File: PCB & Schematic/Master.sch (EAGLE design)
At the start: 24 parts, among them IC1 MAX705CUA, M1 ARDUINO_R3_ICSP_NODIM, X1 MAB5SH, X2 MAB5SH

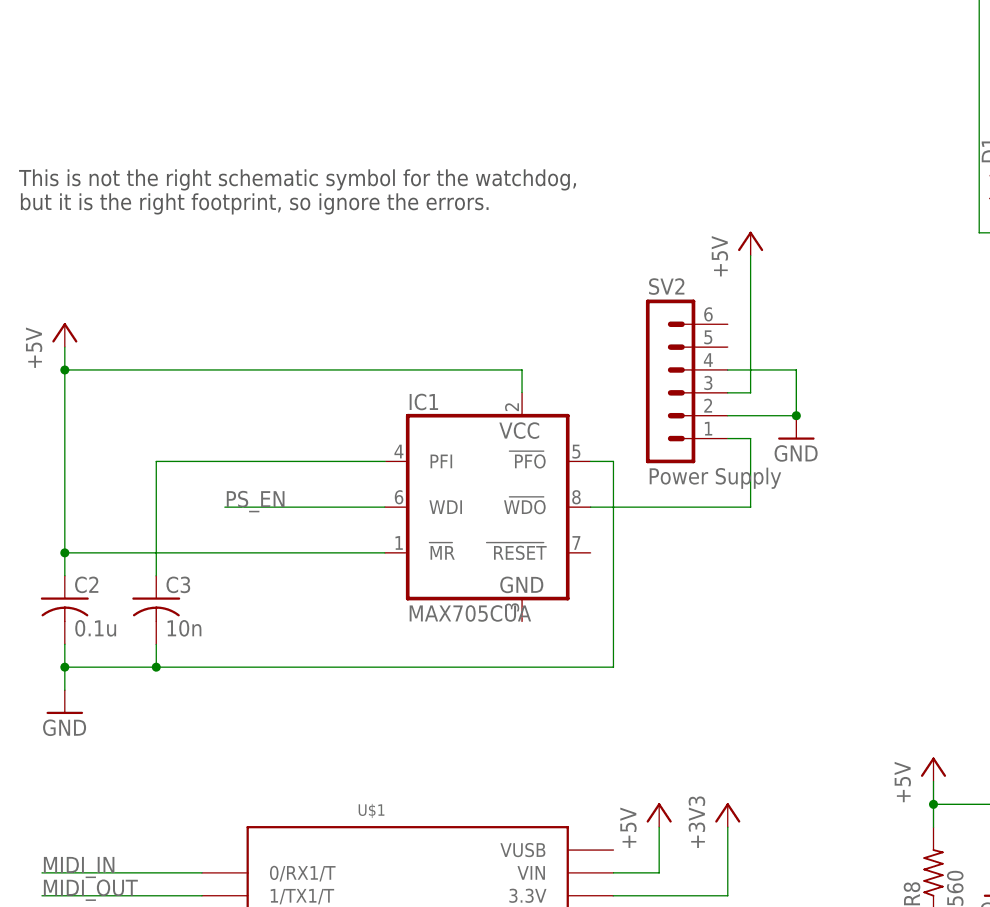
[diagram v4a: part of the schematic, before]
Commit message: Make the correct part for the watchdog.
This is much cleaner.
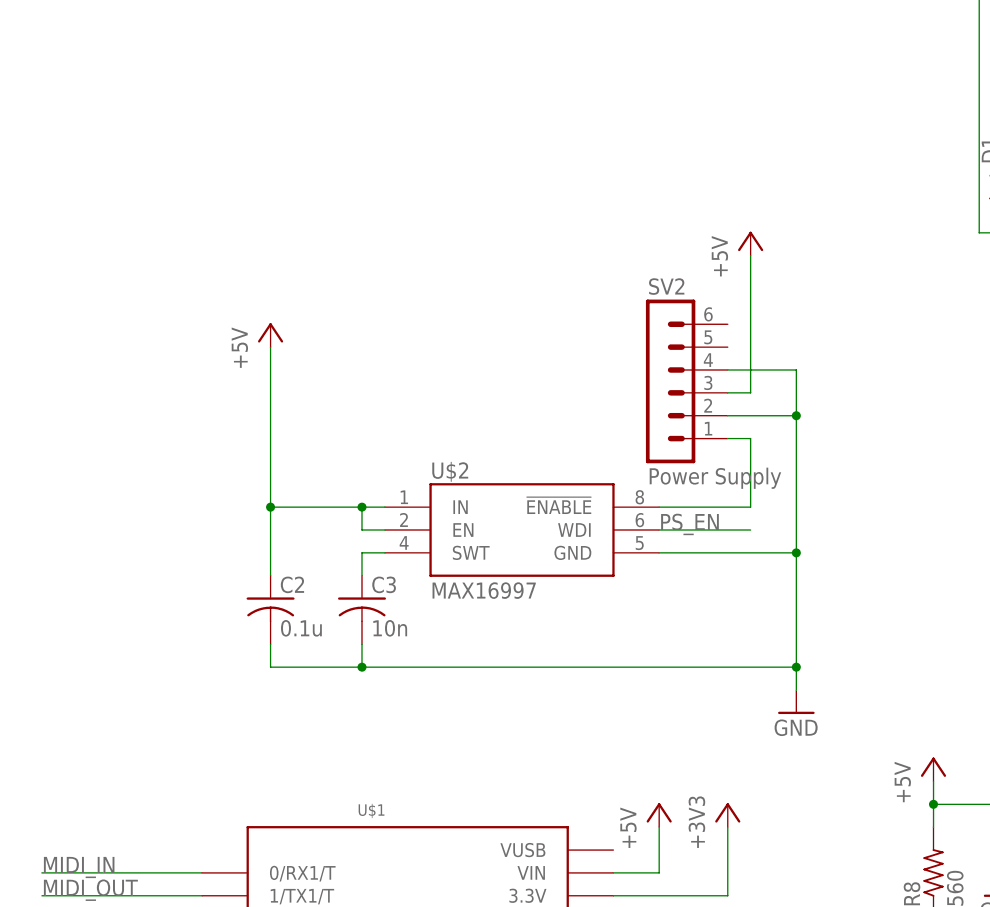
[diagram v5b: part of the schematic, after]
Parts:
- removed IC1: MAX705CUA, maxim:MAX705CUA
- added U$2: MAX16997, DAVe3283:MAX16997
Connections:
- removed net N$15: C3.1, IC1.PFI
- new net N$8: C3.1, U$2.SWT
- net +5V: now also U$2.EN, U$2.IN; no longer IC1.MR, IC1.VCC
- net GND: now also U$2.GND; no longer IC1.PFO
- net N$11: now also U$2.!ENABLE; no longer IC1.WDO
- net PS_EN: now also U$2.WDI; no longer IC1.WDI
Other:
- note removed: "This is not the right schematic symbol for the watchdog, but it is the right footprint, so ignore the errors."
- moved on the sheet: C2, C3
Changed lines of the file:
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@@
 <part name="GND5" library="supply1" deviceset="GNDINT" device=""/>
 <part name="SV2" library="con-lstb" deviceset="MA06-1" device="" value="Power Supply"/>
-<part name="GND6" library="supply1" deviceset="GND" device=""/>
 <part name="P+4" library="supply1" deviceset="+5V" device=""/>
-<part name="IC1" library="maxim" deviceset="MAX705CUA" device=""/>
 <part name="P+7" library="supply1" deviceset="+5V" device=""/>
 <part name="C2" library="resistor" deviceset="C-US" device="C0805" value="0.1u"/>
 <part name="GND7" library="supply1" deviceset="GND" device=""/>
 <part name="C3" library="resistor" deviceset="C-US" device="C0805" value="10n"/>
+<part name="U$2" library="DAVe3283" deviceset="MAX16997" device=""/>
 </parts>
 <sheets>
 <sheet>
 <plain>
-<text x="0" y="139.7" size="1.778" layer="97">This is not the right schematic symbol for the watchdog,
-but it is the right footprint, so ignore the errors.</text>
 </plain>
 <instances>
@@
 <instance part="GND5" gate="G$1" x="147.32" y="35.56"/>
 <instance part="SV2" gate="1" x="71.12" y="121.92"/>
-<instance part="GND6" gate="1" x="86.36" y="114.3"/>
 <instance part="P+4" gate="1" x="81.28" y="137.16"/>
-<instance part="IC1" gate="G$1" x="50.8" y="106.68"/>
-<instance part="P+7" gate="1" x="5.08" y="127"/>
-<instance part="C2" gate="G$1" x="5.08" y="96.52"/>
-<instance part="GND7" gate="1" x="5.08" y="83.82"/>
-<instance part="C3" gate="G$1" x="15.24" y="96.52"/>
+<instance part="P+7" gate="1" x="27.94" y="127"/>
+<instance part="C2" gate="G$1" x="27.94" y="96.52"/>
+<instance part="GND7" gate="1" x="86.36" y="83.82"/>
+<instance part="C3" gate="G$1" x="38.1" y="96.52"/>
+<instance part="U$2" gate="G$1" x="55.88" y="104.14"/>
 </instances>
 <busses>
@@
 </segment>
 <segment>
-<pinref part="GND6" gate="1" pin="GND"/>
+<pinref part="C2" gate="G$1" pin="2"/>
+<wire x1="38.1" y1="88.9" x2="27.94" y2="88.9" width="0.1524" layer="91"/>
+<wire x1="27.94" y1="88.9" x2="27.94" y2="91.44" width="0.1524" layer="91"/>
+<pinref part="C3" gate="G$1" pin="2"/>
+<wire x1="38.1" y1="91.44" x2="38.1" y2="88.9" width="0.1524" layer="91"/>
 <pinref part="SV2" gate="1" pin="2"/>
 <wire x1="86.36" y1="116.84" x2="78.74" y2="116.84" width="0.1524" layer="91"/>
-<junction x="86.36" y="116.84"/>
 <pinref part="SV2" gate="1" pin="4"/>
 <wire x1="78.74" y1="121.92" x2="86.36" y2="121.92" width="0.1524" layer="91"/>
 <wire x1="86.36" y1="121.92" x2="86.36" y2="116.84" width="0.1524" layer="91"/>
-</segment>
-<segment>
-<pinref part="IC1" gate="G$1" pin="PFO"/>
-<wire x1="63.5" y1="111.76" x2="66.04" y2="111.76" width="0.1524" layer="91"/>
-<wire x1="66.04" y1="111.76" x2="66.04" y2="88.9" width="0.1524" layer="91"/>
-<pinref part="C2" gate="G$1" pin="2"/>
-<wire x1="66.04" y1="88.9" x2="15.24" y2="88.9" width="0.1524" layer="91"/>
-<wire x1="15.24" y1="88.9" x2="5.08" y2="88.9" width="0.1524" layer="91"/>
-<wire x1="5.08" y1="88.9" x2="5.08" y2="91.44" width="0.1524" layer="91"/>
-<wire x1="5.08" y1="86.36" x2="5.08" y2="88.9" width="0.1524" layer="91"/>
-<junction x="5.08" y="88.9"/>
+<pinref part="U$2" gate="G$1" pin="GND"/>
+<wire x1="71.12" y1="101.6" x2="86.36" y2="101.6" width="0.1524" layer="91"/>
+<wire x1="86.36" y1="101.6" x2="86.36" y2="116.84" width="0.1524" layer="91"/>
+<junction x="86.36" y="116.84"/>
+<wire x1="38.1" y1="88.9" x2="86.36" y2="88.9" width="0.1524" layer="91"/>
+<wire x1="86.36" y1="88.9" x2="86.36" y2="101.6" width="0.1524" layer="91"/>
+<junction x="38.1" y="88.9"/>
+<junction x="86.36" y="101.6"/>
 <pinref part="GND7" gate="1" pin="GND"/>
-<pinref part="C3" gate="G$1" pin="2"/>
-<wire x1="15.24" y1="91.44" x2="15.24" y2="88.9" width="0.1524" layer="91"/>
-<junction x="15.24" y="88.9"/>
+<wire x1="86.36" y1="86.36" x2="86.36" y2="88.9" width="0.1524" layer="91"/>
+<junction x="86.36" y="88.9"/>
 </segment>
 </net>
@@
 <pinref part="P+7" gate="1" pin="+5V"/>
 <pinref part="C2" gate="G$1" pin="1"/>
-<wire x1="5.08" y1="124.46" x2="5.08" y2="121.92" width="0.1524" layer="91"/>
-<pinref part="IC1" gate="G$1" pin="MR"/>
-<wire x1="5.08" y1="121.92" x2="5.08" y2="101.6" width="0.1524" layer="91"/>
-<wire x1="5.08" y1="101.6" x2="5.08" y2="99.06" width="0.1524" layer="91"/>
-<wire x1="40.64" y1="101.6" x2="5.08" y2="101.6" width="0.1524" layer="91"/>
-<junction x="5.08" y="101.6"/>
-<pinref part="IC1" gate="G$1" pin="VCC"/>
-<wire x1="55.88" y1="119.38" x2="55.88" y2="121.92" width="0.1524" layer="91"/>
-<wire x1="55.88" y1="121.92" x2="5.08" y2="121.92" width="0.1524" layer="91"/>
-<junction x="5.08" y="121.92"/>
+<wire x1="27.94" y1="124.46" x2="27.94" y2="106.68" width="0.1524" layer="91"/>
+<pinref part="U$2" gate="G$1" pin="IN"/>
+<wire x1="27.94" y1="106.68" x2="27.94" y2="99.06" width="0.1524" layer="91"/>
+<wire x1="40.64" y1="106.68" x2="38.1" y2="106.68" width="0.1524" layer="91"/>
+<junction x="27.94" y="106.68"/>
+<pinref part="U$2" gate="G$1" pin="EN"/>
+<wire x1="38.1" y1="106.68" x2="27.94" y2="106.68" width="0.1524" layer="91"/>
+<wire x1="40.64" y1="104.14" x2="38.1" y2="104.14" width="0.1524" layer="91"/>
+<wire x1="38.1" y1="104.14" x2="38.1" y2="106.68" width="0.1524" layer="91"/>
+<junction x="38.1" y="106.68"/>
 </segment>
 </net>
@@
 </segment>
 <segment>
-<pinref part="IC1" gate="G$1" pin="WDI"/>
-<wire x1="40.64" y1="106.68" x2="22.86" y2="106.68" width="0.1524" layer="91"/>
-<label x="22.86" y="106.68" size="1.778" layer="95"/>
+<wire x1="81.28" y1="104.14" x2="71.12" y2="104.14" width="0.1524" layer="91"/>
+<label x="71.12" y="104.14" size="1.778" layer="95"/>
+<pinref part="U$2" gate="G$1" pin="WDI"/>
 </segment>
 <segment>
@@
 </segment>
 </net>
-<net name="N$15" class="0">
-<segment>
-<pinref part="C3" gate="G$1" pin="1"/>
-<wire x1="15.24" y1="99.06" x2="15.24" y2="111.76" width="0.1524" layer="91"/>
-<pinref part="IC1" gate="G$1" pin="PFI"/>
-<wire x1="15.24" y1="111.76" x2="40.64" y2="111.76" width="0.1524" layer="91"/>
-</segment>
-</net>
 <net name="N$11" class="0">
 <segment>
-<pinref part="IC1" gate="G$1" pin="WDO"/>
-<wire x1="63.5" y1="106.68" x2="81.28" y2="106.68" width="0.1524" layer="91"/>
 <wire x1="81.28" y1="106.68" x2="81.28" y2="114.3" width="0.1524" layer="91"/>
 <pinref part="SV2" gate="1" pin="1"/>
 <wire x1="81.28" y1="114.3" x2="78.74" y2="114.3" width="0.1524" layer="91"/>
+<pinref part="U$2" gate="G$1" pin="!ENABLE"/>
+<wire x1="71.12" y1="106.68" x2="81.28" y2="106.68" width="0.1524" layer="91"/>
+</segment>
+</net>
+<net name="N$8" class="0">
+<segment>
+<pinref part="U$2" gate="G$1" pin="SWT"/>
+<pinref part="C3" gate="G$1" pin="1"/>
+<wire x1="40.64" y1="101.6" x2="38.1" y2="101.6" width="0.1524" layer="91"/>
+<wire x1="38.1" y1="101.6" x2="38.1" y2="99.06" width="0.1524" layer="91"/>
 </segment>
 </net>
@@
 </schematic>
 </drawing>
-<compatibility>
-<note version="6.3" minversion="6.2.2" severity="warning">
-Since Version 6.2.2 text objects can contain more than one line,
-which will not be processed correctly with this version.
-</note>
-</compatibility>
 </eagle>

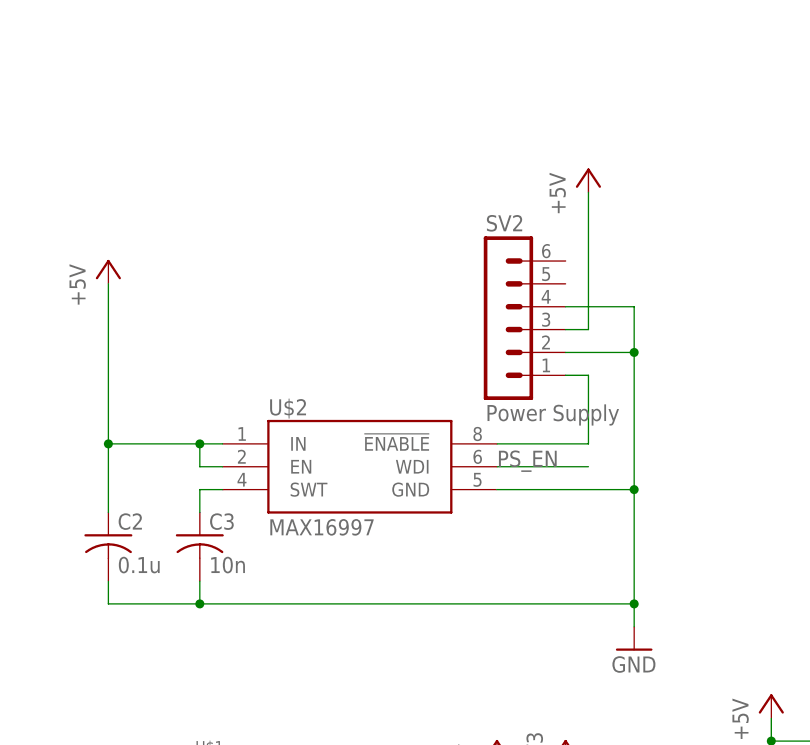
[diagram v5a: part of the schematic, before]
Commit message: Power connector now 4 pin. Add doorbell notes.
The 6 pin connector was unnecessary, and risked confusion with the
slave board connector.

Added some notes on the cheap wireless doorbell I bought to
integrate with the chimes.
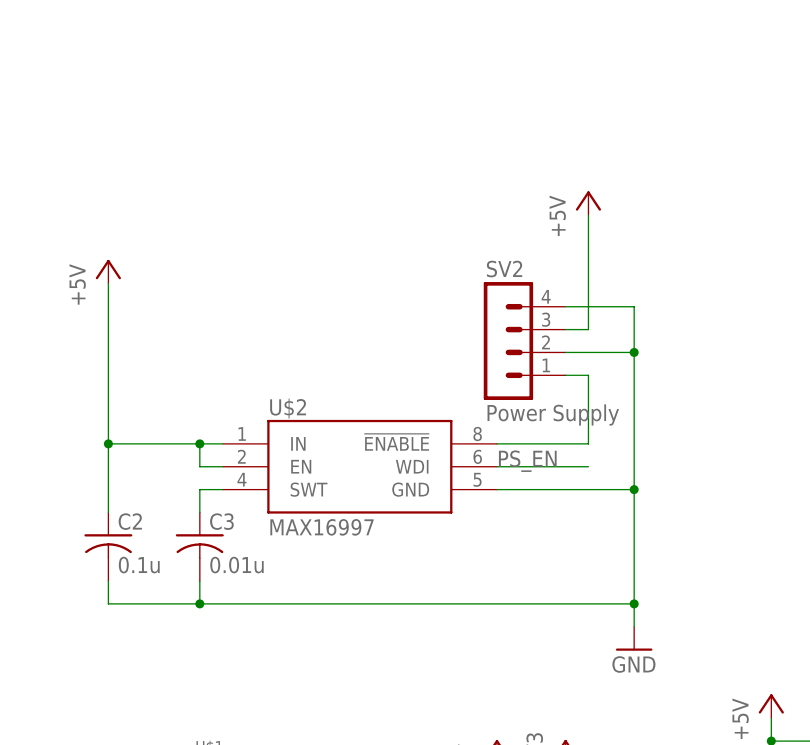
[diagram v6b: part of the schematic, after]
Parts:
- C3: value 10n -> 0.01u
- SV2: device con-lstb:MA06-1 -> con-lstb:MA04-1
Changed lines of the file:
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@@
 <part name="VCC1" library="supply1" deviceset="VCCINT" device=""/>
 <part name="GND5" library="supply1" deviceset="GNDINT" device=""/>
-<part name="SV2" library="con-lstb" deviceset="MA06-1" device="" value="Power Supply"/>
+<part name="SV2" library="con-lstb" deviceset="MA04-1" device="" value="Power Supply"/>
 <part name="P+4" library="supply1" deviceset="+5V" device=""/>
 <part name="P+7" library="supply1" deviceset="+5V" device=""/>
 <part name="C2" library="resistor" deviceset="C-US" device="C0805" value="0.1u"/>
 <part name="GND7" library="supply1" deviceset="GND" device=""/>
-<part name="C3" library="resistor" deviceset="C-US" device="C0805" value="10n"/>
+<part name="C3" library="resistor" deviceset="C-US" device="C0805" value="0.01u"/>
 <part name="U$2" library="DAVe3283" deviceset="MAX16997" device=""/>
 </parts>
@@
 <instance part="VCC1" gate="G$1" x="149.86" y="99.06"/>
 <instance part="GND5" gate="G$1" x="147.32" y="35.56"/>
-<instance part="SV2" gate="1" x="71.12" y="121.92"/>
-<instance part="P+4" gate="1" x="81.28" y="137.16"/>
+<instance part="SV2" gate="1" x="71.12" y="119.38"/>
+<instance part="P+4" gate="1" x="81.28" y="134.62"/>
 <instance part="P+7" gate="1" x="27.94" y="127"/>
 <instance part="C2" gate="G$1" x="27.94" y="96.52"/>
@@
 <wire x1="78.74" y1="119.38" x2="81.28" y2="119.38" width="0.1524" layer="91"/>
 <pinref part="P+4" gate="1" pin="+5V"/>
-<wire x1="81.28" y1="134.62" x2="81.28" y2="119.38" width="0.1524" layer="91"/>
+<wire x1="81.28" y1="132.08" x2="81.28" y2="119.38" width="0.1524" layer="91"/>
 </segment>
 <segment>

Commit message: Add connector for wireless doorbell.
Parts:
- added SV3: Doorbell, con-lstb:MA03-1
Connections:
- new net DOORBELL_IN: SV3.2, U$1.2
- net +5V: now also SV3.3
- net GND: now also SV3.1
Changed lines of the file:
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@@
 <part name="C3" library="resistor" deviceset="C-US" device="C0805" value="0.01u"/>
 <part name="U$2" library="DAVe3283" deviceset="MAX16997" device=""/>
+<part name="SV3" library="con-lstb" deviceset="MA03-1" device="" value="Doorbell"/>
+<part name="GND6" library="supply1" deviceset="GND" device=""/>
+<part name="P+8" library="supply1" deviceset="+5V" device=""/>
 </parts>
 <sheets>
@@
 <instance part="C3" gate="G$1" x="38.1" y="96.52"/>
 <instance part="U$2" gate="G$1" x="55.88" y="104.14"/>
+<instance part="SV3" gate="G$1" x="-10.16" y="60.96"/>
+<instance part="GND6" gate="1" x="0" y="53.34"/>
+<instance part="P+8" gate="1" x="0" y="73.66"/>
 </instances>
 <busses>
@@
 <junction x="86.36" y="88.9"/>
 </segment>
+<segment>
+<pinref part="SV3" gate="G$1" pin="1"/>
+<pinref part="GND6" gate="1" pin="GND"/>
+<wire x1="-2.54" y1="58.42" x2="0" y2="58.42" width="0.1524" layer="91"/>
+<wire x1="0" y1="58.42" x2="0" y2="55.88" width="0.1524" layer="91"/>
+</segment>
 </net>
 <net name="+5V" class="0">
@@
 <wire x1="38.1" y1="104.14" x2="38.1" y2="106.68" width="0.1524" layer="91"/>
 <junction x="38.1" y="106.68"/>
+</segment>
+<segment>
+<pinref part="SV3" gate="G$1" pin="3"/>
+<pinref part="P+8" gate="1" pin="+5V"/>
+<wire x1="-2.54" y1="63.5" x2="0" y2="63.5" width="0.1524" layer="91"/>
+<wire x1="0" y1="63.5" x2="0" y2="71.12" width="0.1524" layer="91"/>
 </segment>
 </net>
@@
 </segment>
 </net>
+<net name="DOORBELL_IN" class="0">
+<segment>
+<pinref part="SV3" gate="G$1" pin="2"/>
+<pinref part="U$1" gate="G$1" pin="2"/>
+<wire x1="-2.54" y1="60.96" x2="20.32" y2="60.96" width="0.1524" layer="91"/>
+<label x="2.54" y="60.96" size="1.778" layer="95"/>
+</segment>
+</net>

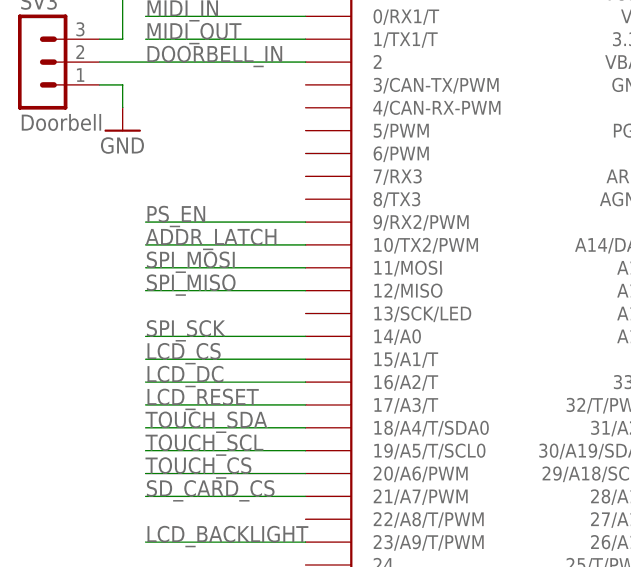
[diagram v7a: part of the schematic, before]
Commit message: Move LCD DC Pin to a physical CS pin on the Teensy.
I failed to notice the library won't support the display if both
CS and DC pins aren't on hardware CS pins. D'oh!
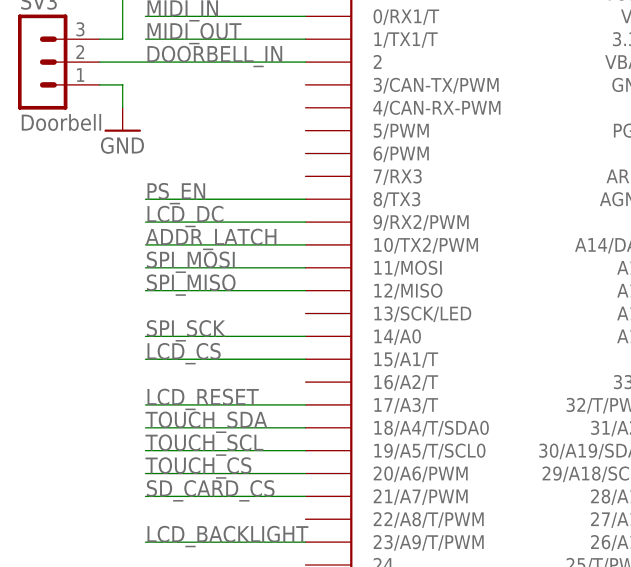
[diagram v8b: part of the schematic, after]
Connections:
- net LCD_DC: now also U$1.9/RX2/PWM; no longer U$1.16/A2/T
- net PS_EN: now also U$1.8/TX3; no longer U$1.9/RX2/PWM
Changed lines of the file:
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@@
 </segment>
 <segment>
-<pinref part="U$1" gate="G$1" pin="9/RX2/PWM"/>
-<wire x1="20.32" y1="43.18" x2="2.54" y2="43.18" width="0.1524" layer="91"/>
-<label x="2.54" y="43.18" size="1.778" layer="95"/>
+<label x="2.54" y="45.72" size="1.778" layer="95"/>
+<pinref part="U$1" gate="G$1" pin="8/TX3"/>
+<wire x1="20.32" y1="45.72" x2="2.54" y2="45.72" width="0.1524" layer="91"/>
 </segment>
 </net>
@@
 </segment>
 <segment>
-<pinref part="U$1" gate="G$1" pin="16/A2/T"/>
-<wire x1="20.32" y1="25.4" x2="2.54" y2="25.4" width="0.1524" layer="91"/>
-<label x="2.54" y="25.4" size="1.778" layer="95"/>
+<pinref part="U$1" gate="G$1" pin="9/RX2/PWM"/>
+<wire x1="20.32" y1="43.18" x2="2.54" y2="43.18" width="0.1524" layer="91"/>
+<label x="2.54" y="43.18" size="1.778" layer="95"/>
 </segment>
 </net>
